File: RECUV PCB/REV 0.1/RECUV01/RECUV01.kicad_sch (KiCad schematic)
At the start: 67 parts, among them J1 USB_C_Receptacle_USB2.0_16P, J2 Screw_Terminal_01x02, J5 RIGHT_ROW, J6 LEFT_ROW, J7 LOW_ROW, Q1 Q_NPN_BEC, Q2 Q_NPN_BEC, SW1 RESET, SW2 BOOT, U1 CH340C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

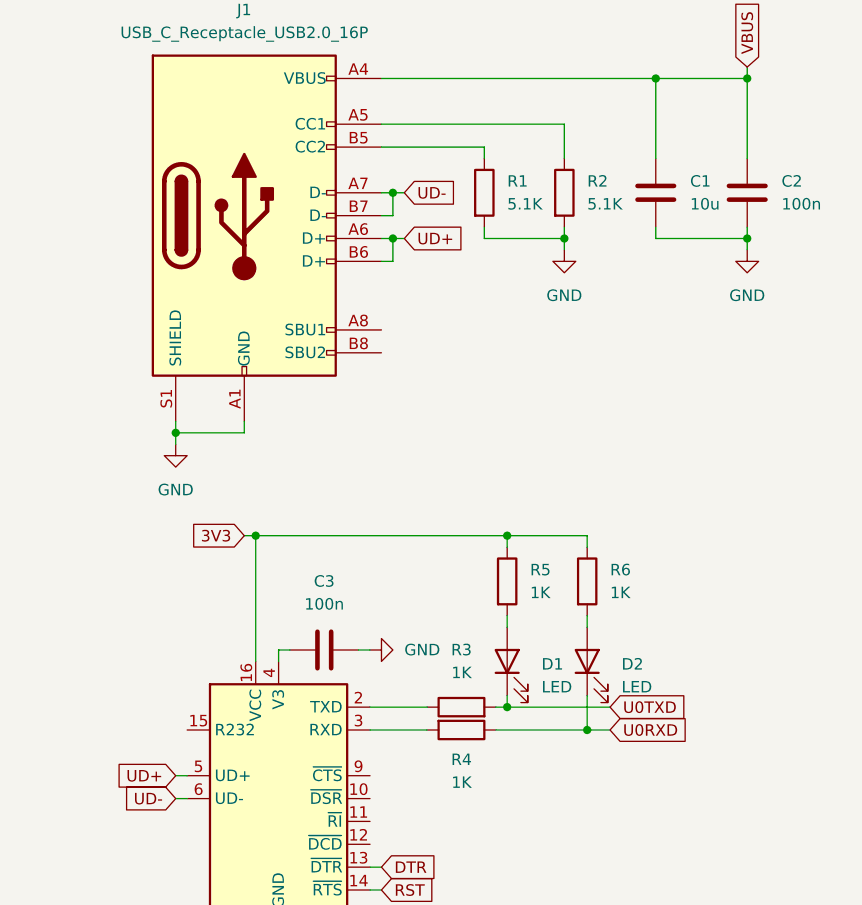
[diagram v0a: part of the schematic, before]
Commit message: Se corrigio TX y RX del CH340 en esquematico
TODO:
Corregirlo en PCB
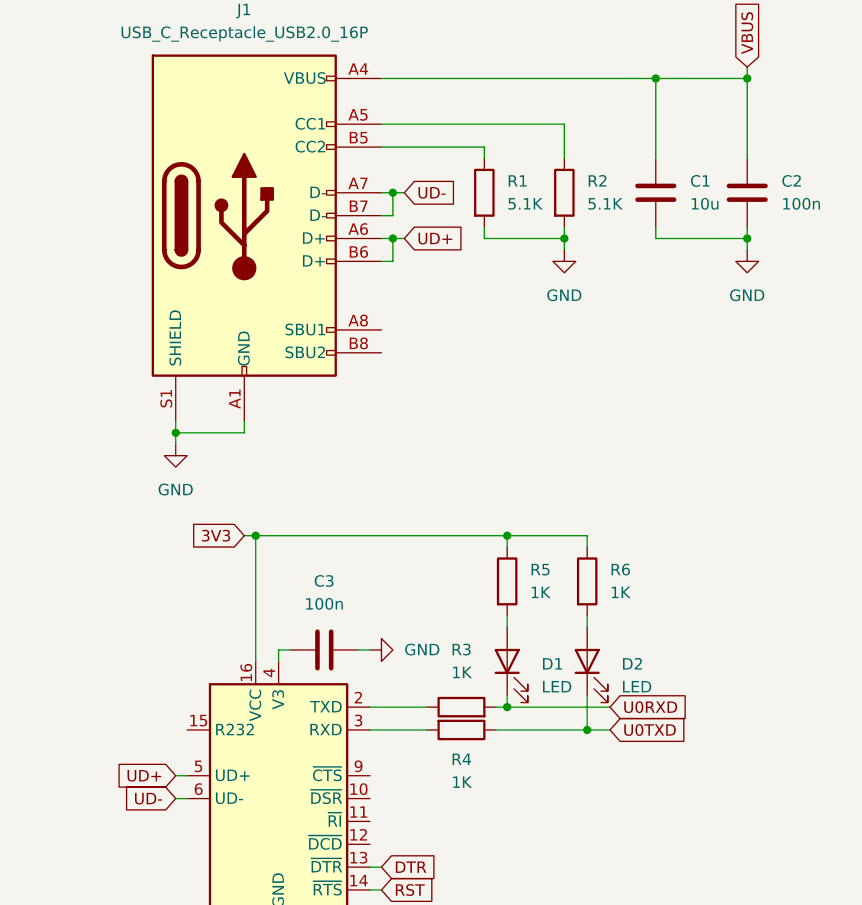
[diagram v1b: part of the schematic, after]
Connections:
- net U0RXD: now also D1.1 (K), R3.2; no longer D2.1 (K), R4.1
- net U0TXD: now also D2.1 (K), R4.1; no longer D1.1 (K), R3.2

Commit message: Added a New RECUV File
- USB-C Added
- UD+ and UD- etiquetes added
- VBUS added
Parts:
- R15: value 10k -> 100k
- U3: value ESP32-S3-WROOM-1 -> ESP32-S3-WROOM-1-N16R8; footprint PCM_Espressif:ESP32-S3-WROOM-1 -> RF_Module:ESP32-S3-WROOM-1; JLCPCB Part # (none) -> C2913202
